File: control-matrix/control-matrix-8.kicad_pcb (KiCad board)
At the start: 2 copper layers, 150 x 30 mm, 30 parts, among them J1 Screw_Terminal_01x02, J2 Screw_Terminal_01x02, J3 Screw_Terminal_01x02, J4 Screw_Terminal_01x02, J5 Screw_Terminal_01x02, J6 Screw_Terminal_01x02, J7 Screw_Terminal_01x02, J8 Screw_Terminal_01x02, J9 Screw_Terminal_01x02, SW1 SW_Rotary_1x12

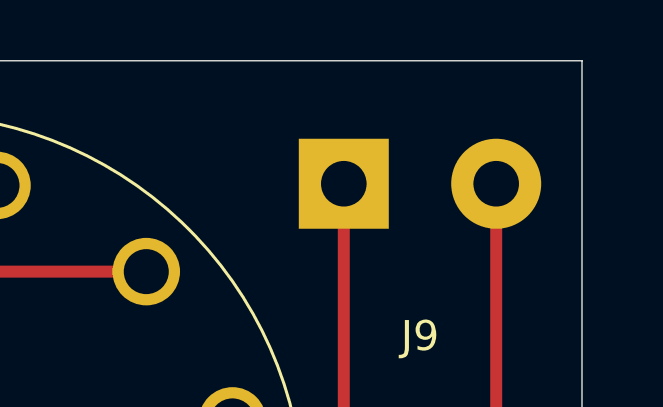
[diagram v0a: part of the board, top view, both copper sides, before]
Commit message: control-matrix: add power input labels on silkscreen
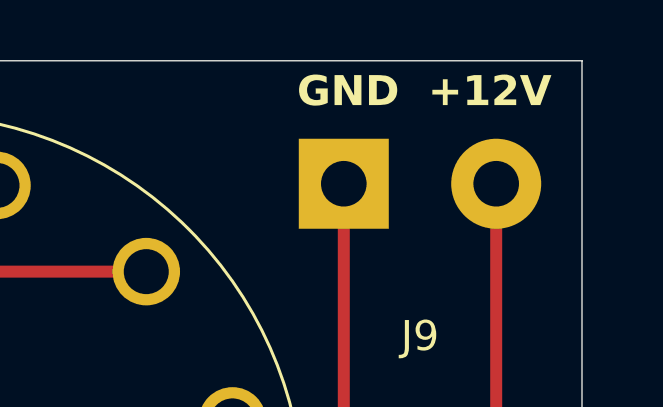
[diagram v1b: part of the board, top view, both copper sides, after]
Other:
- board text added: "GND +12V"
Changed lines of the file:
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@@
 		(layer "Edge.Cuts")
+	)
+	(gr_text "GND  +12V"
+		(at 200.5 81.6 0)
+		(layer "F.SilkS")
+		(effects
+			(font
+				(size 1 1)
+				(thickness 0.2)
+				(bold yes)
+			)
+			(justify left bottom)
+		)
 	)
 	(segment

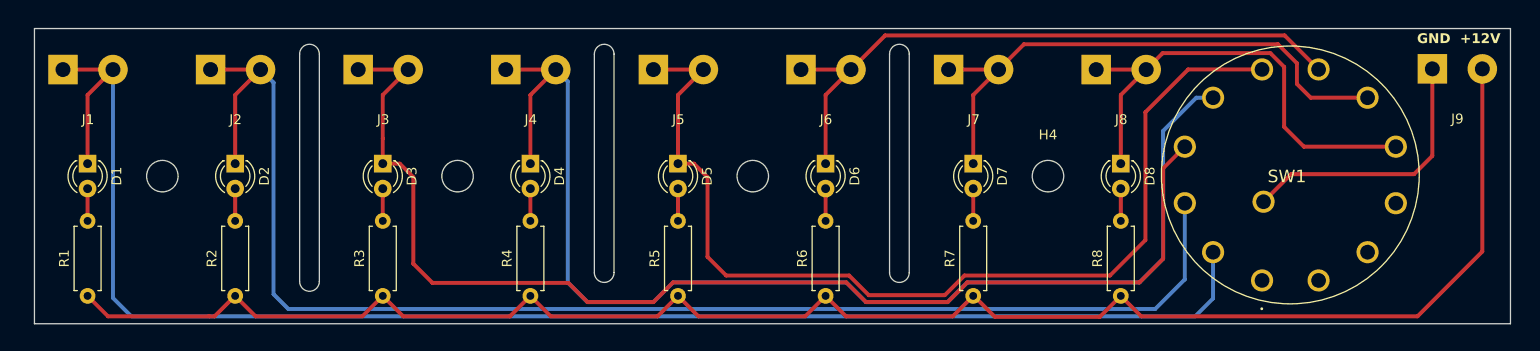
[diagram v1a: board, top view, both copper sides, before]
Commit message: control-matrix: add ground planes
This avoids having to etch too much copper.
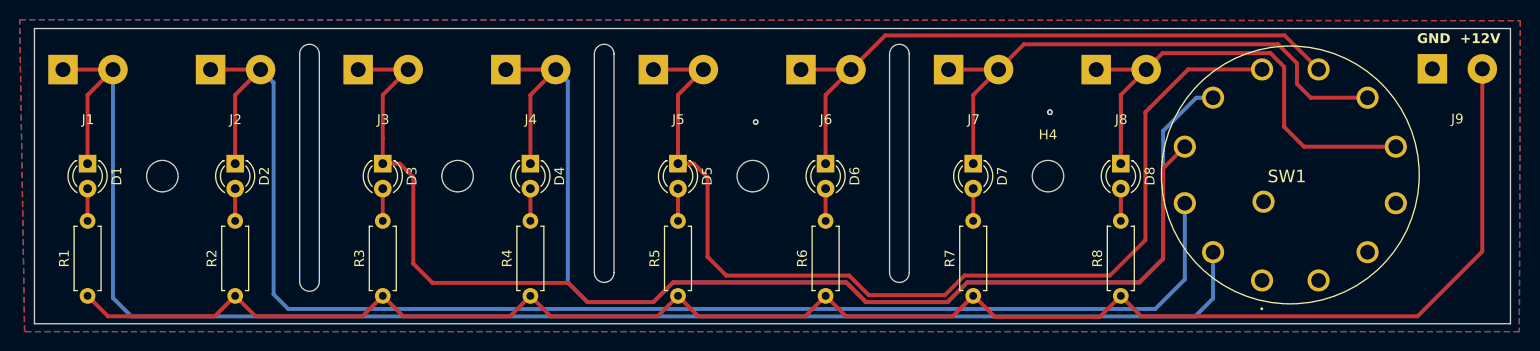
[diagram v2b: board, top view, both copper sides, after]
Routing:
- net GND: track 27.9 -> 0.00 mm, vias 0 -> 2
- added copper zone on B.Cu, net GND
- added copper zone on F.Cu, net GND
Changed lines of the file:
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@@
 		(net 14)
 	)
-	(segment
-		(start 202.06 92.94)
-		(end 200.2 94.8)
-		(width 0.4)
-		(layer "F.Cu")
+	(via
+		(at 163.2 88.5)
+		(size 0.6)
+		(drill 0.3)
+		(layers "F.Cu" "B.Cu")
+		(free yes)
 		(net 15)
 	)
-	(segment
-		(start 202.06 84.1)
-		(end 202.06 92.94)
-		(width 0.4)
-		(layer "F.Cu")
-		(net 15)
-	)
-	(segment
-		(start 200.2 94.8)
-		(end 187.70533 94.8)
-		(width 0.4)
-		(layer "F.Cu")
-		(net 15)
-	)
-	(segment
-		(start 187.70533 94.8)
-		(end 184.90475 97.60058)
-		(width 0.4)
-		(layer "F.Cu")
+	(via
+		(at 133.3 89.5)
+		(size 0.6)
+		(drill 0.3)
+		(layers "F.Cu" "B.Cu")
+		(free yes)
 		(net 15)
 	)
@@
 		(net 22)
 	)
+	(zone
+		(net 15)
+		(net_name "GND")
+		(layers "F.Cu" "B.Cu")
+		(hatch edge 0.5)
+		(connect_pads
+			(clearance 0.5)
+		)
+		(min_thickness 0.25)
+		(filled_areas_thickness no)
+		(fill yes
+			(thermal_gap 0.5)
+			(thermal_bridge_width 0.5)
+		)
+		(polygon
+			(pts
+				(xy 58.5 79.1) (xy 211 79.2) (xy 210.9 110.8) (xy 59 110.8)
+			)
+		)
+	)
 	(group ""
